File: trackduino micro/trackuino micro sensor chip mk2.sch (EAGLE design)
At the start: 41 parts, among them IC2 74AHC1G125DBV, SW1 SPST_TACT-KMR2, U1 ATMEGA168MLF, Y1 16MHZ

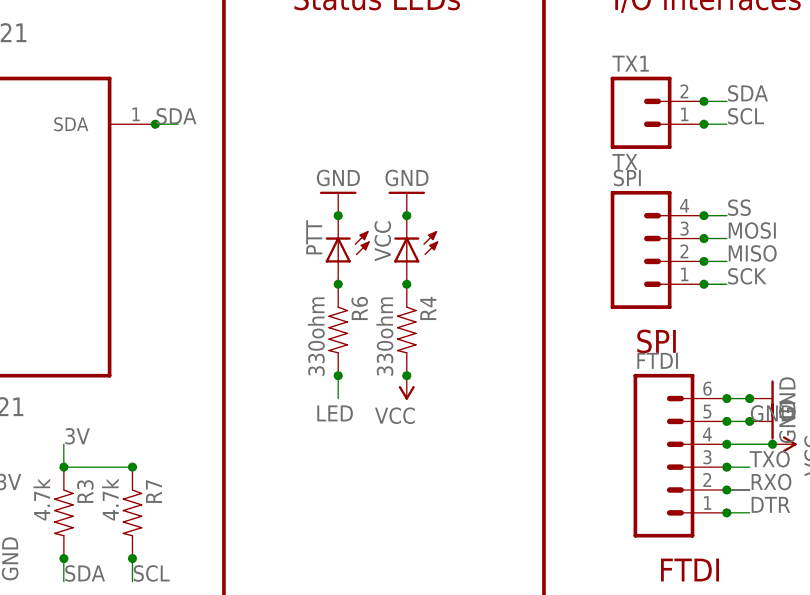
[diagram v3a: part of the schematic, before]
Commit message: tx rx 2mm headers
replaced .1” serial headers on chip and non chip version with 2mm
headers
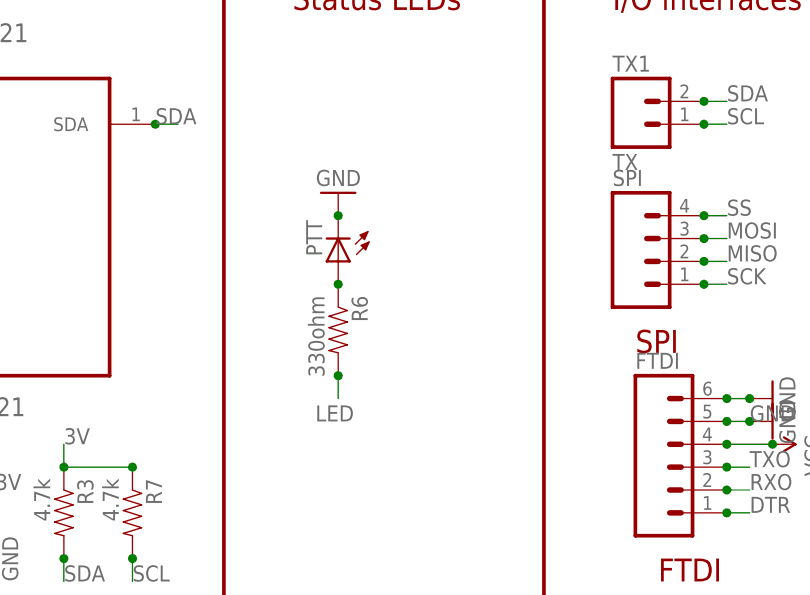
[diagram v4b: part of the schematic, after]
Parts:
- removed R4: 330ohm, SparkFun-Resistors:RESISTOR0805-RES
- removed VCC: (no value), adafruit:LEDCHIP-LED0805
- RX, TX: device SparkFun-Connectors:M02PTH -> SparkFun-Connectors:M02JST-PTH-VERT
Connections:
- removed net N$8: R4.1, VCC.A
- net GND: no longer VCC.C
- net VCC: no longer R4.2
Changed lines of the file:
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@@
 <part name="SUPPLY4" library="SparkFun-Aesthetics" deviceset="VCC" device=""/>
 <part name="SUPPLY5" library="SparkFun-Aesthetics" deviceset="VCC" device=""/>
-<part name="VCC" library="adafruit" deviceset="LED" device="CHIP-LED0805"/>
-<part name="R4" library="SparkFun-Resistors" deviceset="RESISTOR" device="0805-RES" value="330ohm"/>
-<part name="GND19" library="SparkFun-Aesthetics" deviceset="GND" device=""/>
-<part name="SUPPLY6" library="SparkFun-Aesthetics" deviceset="VCC" device=""/>
 <part name="FTDI" library="SparkFun-Connectors" deviceset="M06" device="NO_SILK_FEMALE_PTH"/>
 <part name="SUPPLY7" library="SparkFun-Aesthetics" deviceset="VCC" device=""/>
@@
 <part name="SUPPLY10" library="SparkFun-Aesthetics" deviceset="VCC" device=""/>
 <part name="C5" library="SparkFun-Capacitors" deviceset="CAP" device="0805" value=".1uf"/>
-<part name="TX" library="SparkFun-Connectors" deviceset="M02" device="PTH" value="TX"/>
+<part name="TX" library="SparkFun-Connectors" deviceset="M02" device="JST-PTH-VERT" value="TX"/>
 <part name="SPI" library="SparkFun-Connectors" deviceset="M04" device="JST-PTH-VERT"/>
 <part name="GND23" library="SparkFun-Aesthetics" deviceset="GND" device=""/>
@@
 <part name="GND1" library="SparkFun-Aesthetics" deviceset="GND" device=""/>
 <part name="GND3" library="SparkFun-Aesthetics" deviceset="GND" device=""/>
-<part name="RX" library="SparkFun-Connectors" deviceset="M02" device="PTH" value="RX"/>
+<part name="RX" library="SparkFun-Connectors" deviceset="M02" device="JST-PTH-VERT" value="RX"/>
 <part name="GND10" library="SparkFun-Aesthetics" deviceset="GND" device=""/>
 <part name="BMP180" library="SparkFun-Sensors" deviceset="BMP180" device=""/>
@@
 <instance part="SUPPLY4" gate="G$1" x="55.88" y="160.02" rot="R90"/>
 <instance part="SUPPLY5" gate="G$1" x="55.88" y="152.4" rot="R90"/>
-<instance part="VCC" gate="G$1" x="167.64" y="76.2" rot="R180"/>
-<instance part="R4" gate="G$1" x="167.64" y="68.58" rot="R270"/>
-<instance part="GND19" gate="1" x="167.64" y="83.82" rot="R180"/>
-<instance part="SUPPLY6" gate="G$1" x="167.64" y="63.5" rot="R180"/>
 <instance part="FTDI" gate="G$1" x="198.12" y="53.34"/>
 <instance part="SUPPLY7" gate="G$1" x="25.4" y="60.96" rot="R90"/>
@@
 </segment>
 <segment>
-<pinref part="VCC" gate="G$1" pin="C"/>
-<pinref part="GND19" gate="1" pin="GND"/>
-<junction x="167.64" y="81.28"/>
-</segment>
-<segment>
 <pinref part="U1" gate="G$1" pin="GND@1"/>
 <pinref part="GND12" gate="1" pin="GND"/>
@@
 <pinref part="SUPPLY5" gate="G$1" pin="VCC"/>
 <junction x="55.88" y="152.4"/>
-</segment>
-<segment>
-<pinref part="R4" gate="G$1" pin="2"/>
-<pinref part="SUPPLY6" gate="G$1" pin="VCC"/>
-<junction x="167.64" y="63.5"/>
 </segment>
 <segment>
@@
 </segment>
 </net>
-<net name="N$8" class="0">
-<segment>
-<pinref part="VCC" gate="G$1" pin="A"/>
-<pinref part="R4" gate="G$1" pin="1"/>
-<junction x="167.64" y="73.66"/>
-</segment>
-</net>

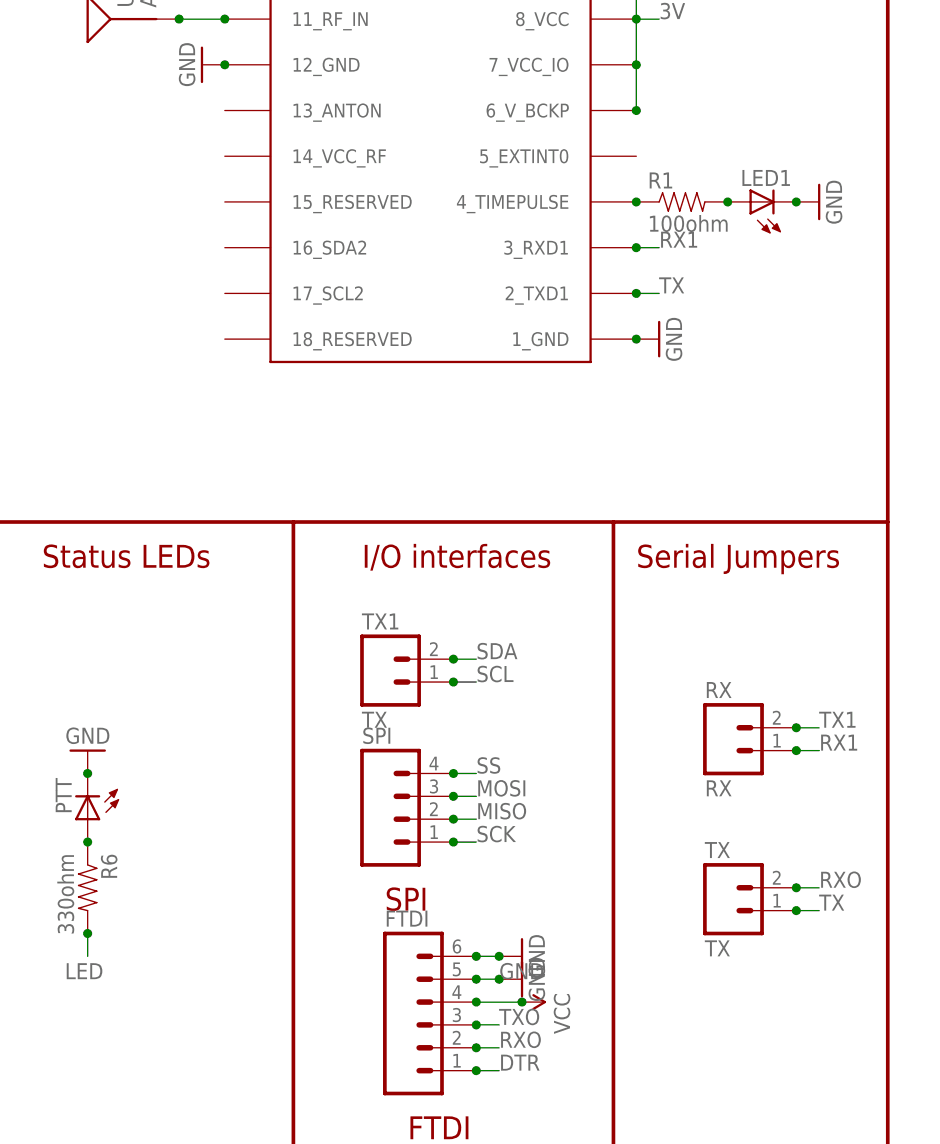
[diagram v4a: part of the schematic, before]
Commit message: Standardized round via
Changed all via on production boards to round, and moved hidden via on
solar board out from under the atmega. Also fixed bom to specify
max-m8q gps.
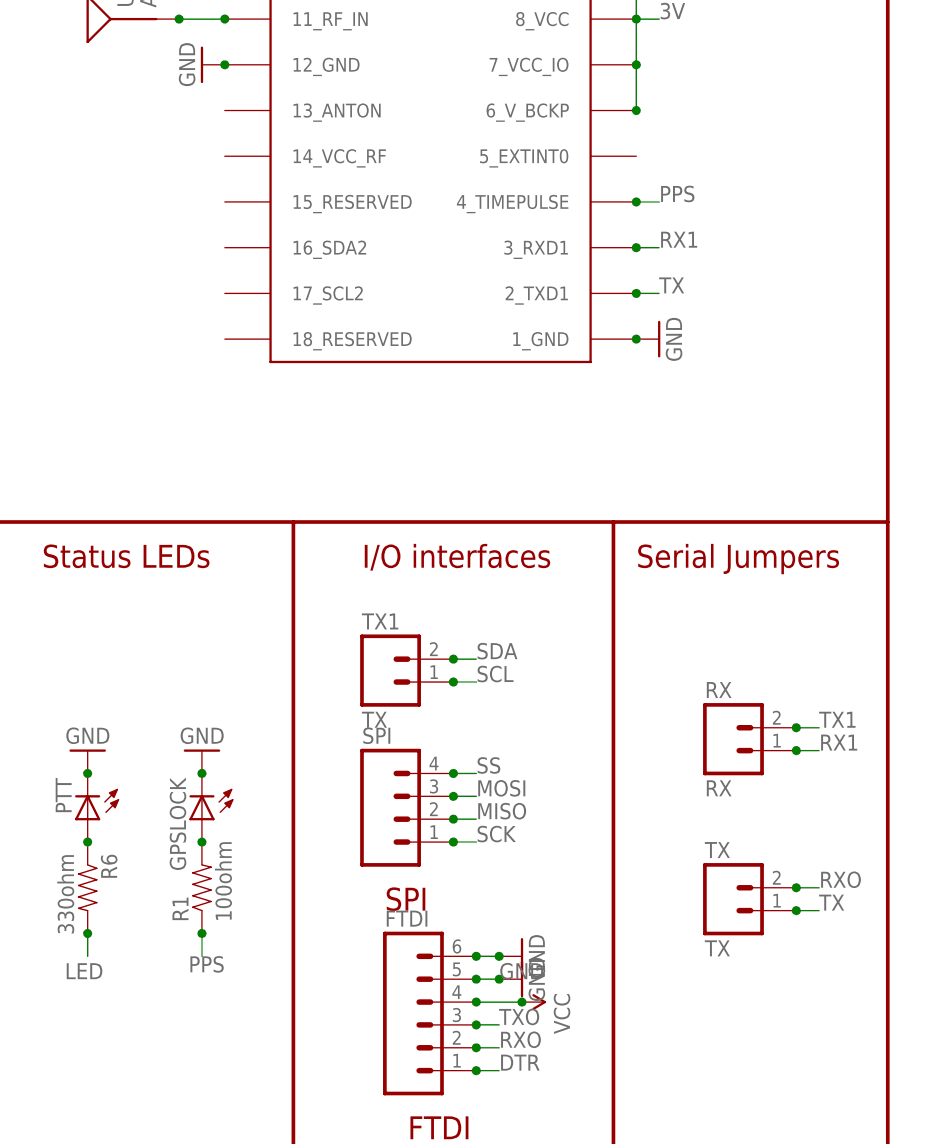
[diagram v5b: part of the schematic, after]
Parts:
- removed LED1: (no value), adafruit:LEDCHIP-LED0805
- added GPSLOCK: (no value), adafruit:LEDCHIP-LED0805
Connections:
- net N$2 renamed PPS
- net GND: now also GPSLOCK.C; no longer LED1.C
- net N$3: now also GPSLOCK.A; no longer LED1.A
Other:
- moved on the sheet: R1
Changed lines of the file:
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@@
 <?xml version="1.0" encoding="utf-8"?>
 <!DOCTYPE eagle SYSTEM "eagle.dtd">
-<eagle version="7.2.0">
+<eagle version="7.1.0">
 <drawing>
 <settings>
@@
 <part name="GND7" library="SparkFun-Aesthetics" deviceset="GND" device=""/>
 <part name="R1" library="SparkFun-Resistors" deviceset="RESISTOR" device="0805-RES" value="100ohm"/>
-<part name="LED1" library="adafruit" deviceset="LED" device="CHIP-LED0805"/>
+<part name="GPSLOCK" library="adafruit" deviceset="LED" device="CHIP-LED0805"/>
 <part name="GND8" library="SparkFun-Aesthetics" deviceset="GND" device=""/>
 <part name="GND9" library="SparkFun-Aesthetics" deviceset="GND" device=""/>
@@
 <instance part="SUPPLY3" gate="G$1" x="109.22" y="132.08" rot="R90"/>
 <instance part="GND7" gate="1" x="106.68" y="127" rot="R270"/>
-<instance part="R1" gate="G$1" x="226.06" y="144.78"/>
-<instance part="LED1" gate="G$1" x="233.68" y="144.78" rot="R90"/>
-<instance part="GND8" gate="1" x="241.3" y="144.78" rot="R90"/>
+<instance part="R1" gate="G$1" x="172.72" y="68.58" rot="R90"/>
+<instance part="GPSLOCK" gate="G$1" x="172.72" y="76.2" rot="R180"/>
+<instance part="GND8" gate="1" x="172.72" y="83.82" rot="R180"/>
 <instance part="GND9" gate="1" x="223.52" y="129.54" rot="R90"/>
 <instance part="GND13" gate="1" x="172.72" y="160.02" rot="R270"/>
@@
 </segment>
 <segment>
-<pinref part="LED1" gate="G$1" pin="C"/>
+<pinref part="GPSLOCK" gate="G$1" pin="C"/>
 <pinref part="GND8" gate="1" pin="GND"/>
-<junction x="238.76" y="144.78"/>
+<junction x="172.72" y="81.28"/>
 </segment>
 <segment>
@@
 <segment>
 <pinref part="R1" gate="G$1" pin="2"/>
-<pinref part="LED1" gate="G$1" pin="A"/>
-<junction x="231.14" y="144.78"/>
+<pinref part="GPSLOCK" gate="G$1" pin="A"/>
+<junction x="172.72" y="73.66"/>
 </segment>
 </net>
@@
 <junction x="25.4" y="43.18"/>
 <pinref part="Y1" gate="G$1" pin="1"/>
-</segment>
-</net>
-<net name="N$2" class="0">
-<segment>
-<pinref part="U$1" gate="G$1" pin="4_TIMEPULSE"/>
-<pinref part="R1" gate="G$1" pin="1"/>
-<junction x="220.98" y="144.78"/>
 </segment>
 </net>
@@
 </segment>
 </net>
+<net name="PPS" class="0">
+<segment>
+<pinref part="U$1" gate="G$1" pin="4_TIMEPULSE"/>
+<wire x1="220.98" y1="144.78" x2="223.52" y2="144.78" width="0.1524" layer="91"/>
+<junction x="220.98" y="144.78"/>
+<label x="223.52" y="144.78" size="1.778" layer="95"/>
+</segment>
+<segment>
+<pinref part="R1" gate="G$1" pin="1"/>
+<wire x1="172.72" y1="63.5" x2="172.72" y2="60.96" width="0.1524" layer="91"/>
+<junction x="172.72" y="63.5"/>
+<label x="175.26" y="60.96" size="1.778" layer="95" rot="R180"/>
+</segment>
+</net>
